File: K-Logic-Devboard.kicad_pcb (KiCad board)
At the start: 2 copper layers, 21 x 51 mm, 33 parts, among them J1 USB_C_Receptacle_USB2.0_14P, J2 Conn_01x20, J3 Conn_01x20, J4 Conn_01x03, SW1 SW_Push, U1 RP2040, U2 MCP1700x-330xxTT, U3 W25Q16JVZPIQ TR, Y1 12 Mhz

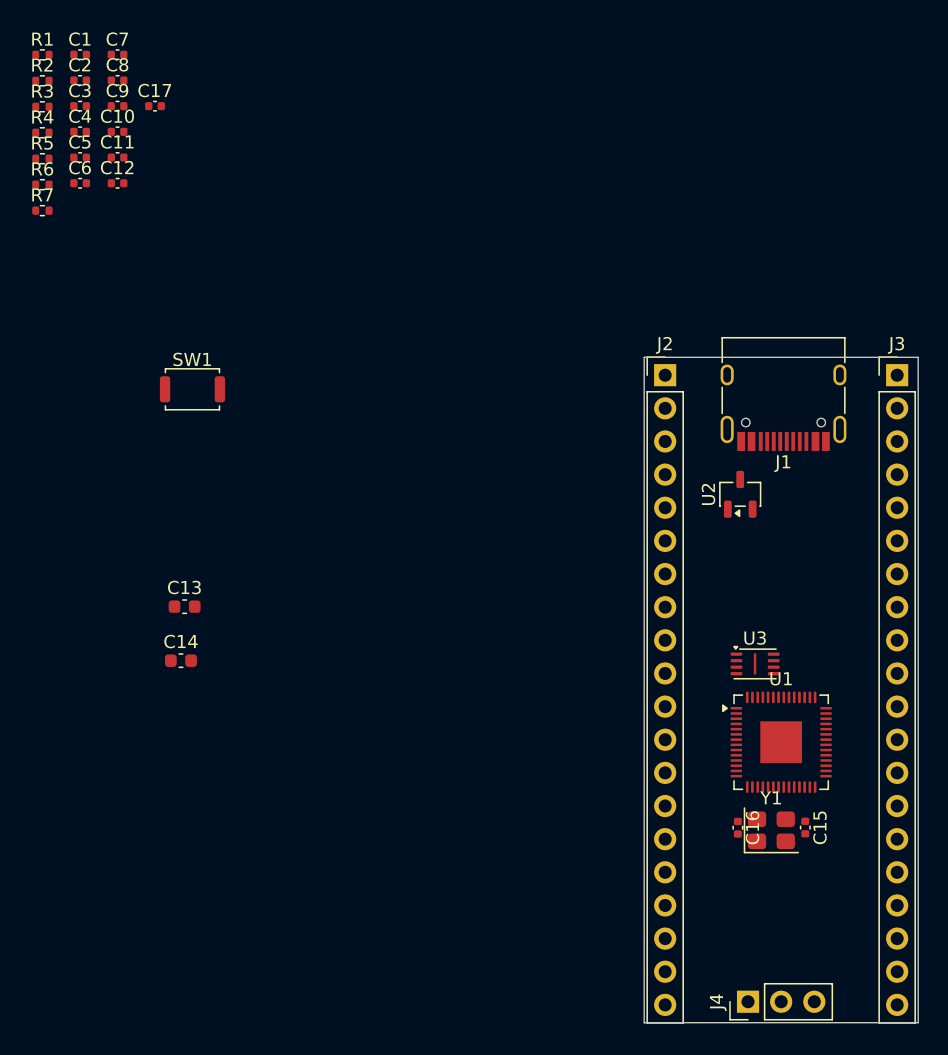
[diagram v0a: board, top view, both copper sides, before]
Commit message: pcb 99.99% done. journals and BOM.
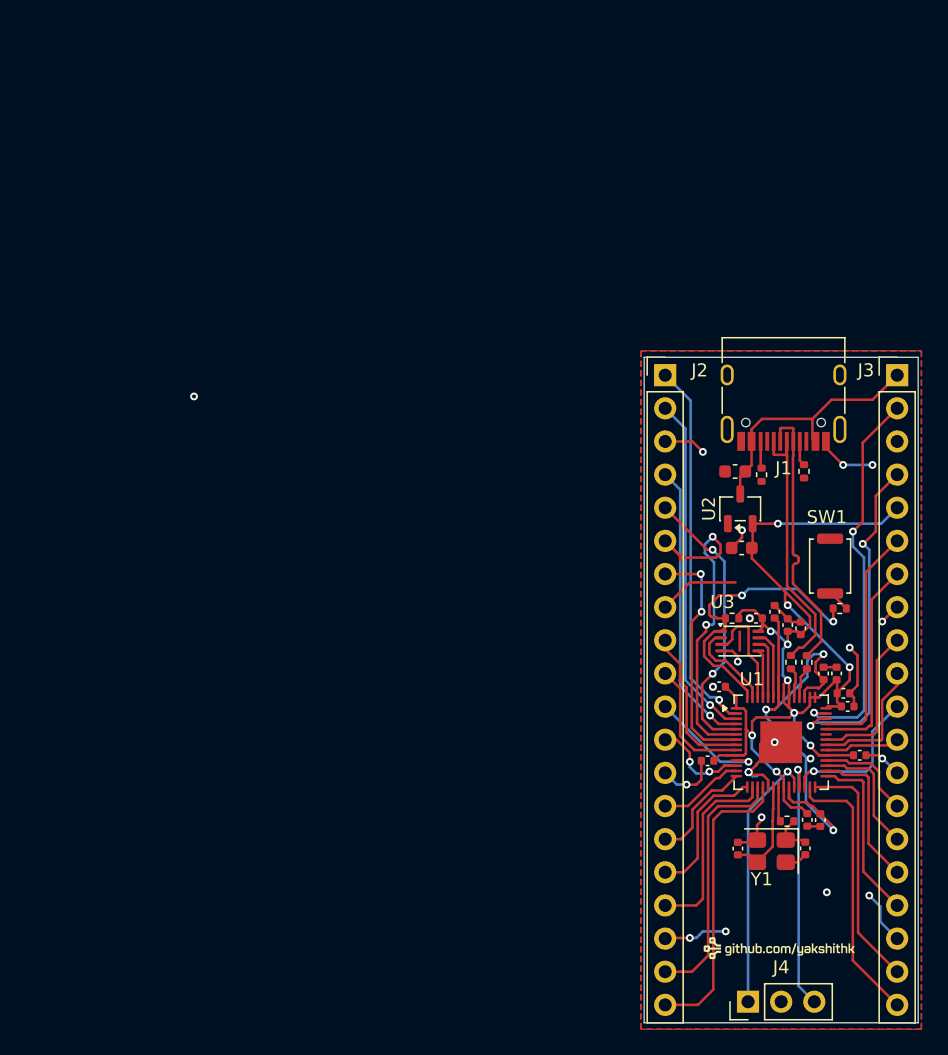
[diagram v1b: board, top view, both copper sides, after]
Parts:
- added G***: LOGO, LOGO, F.Cu at (91.3, 89.3)
- added G***: LOGO, LOGO, B.Cu at (91.8, 68.8)
- moved C8 77.5 mm to (93.5, 79.5), turned to -90 degrees
- moved R5 76.4 mm to (91.9, 79.6), turned to 180 degrees
- moved C1 76.3 mm to (96.3, 69.8)
- moved C2 75.9 mm to (96.6, 70.8)
- moved C5 75.3 mm to (97.5, 74.5)
- moved C11 74.0 mm to (94.5, 79.5), turned to -90 degrees
- moved C7 72.7 mm to (95.8, 68.2), turned to 90 degrees
- moved R3 72.4 mm to (93.5, 67.4), turned to 90 degrees
- moved R4 70.3 mm to (92.2, 67.4), turned to 90 degrees
- moved R6 69.2 mm to (96.0, 63.2), turned to 180 degrees
- moved C3 68.2 mm to (93.0, 64.8), turned to 90 degrees
- moved C10 68.2 mm to (94.8, 68.2), turned to 90 degrees
- moved R1 66.5 mm to (93.2, 52.7), turned to -90 degrees
- moved C4 66.1 mm to (92.0, 64.5), turned to 90 degrees
- moved C6 65.4 mm to (85.9, 74.9), turned to 180 degrees
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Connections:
- R3 pad 2: USB_D+ -> USB_D-
- R4 pad 2: USB_D- -> USB_D+
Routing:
- net +3V3: track 0.00 -> 87.8 mm, vias 0 -> 10
- net GND: track 0.00 -> 58.1 mm, vias 0 -> 19
- net +1V1: track 0.00 -> 38.3 mm, vias 0 -> 4
- net GPIO29_ADC3: track 0.00 -> 30.1 mm, vias 0 -> 2
- net GPIO0: track 0.00 -> 28.8 mm, vias 0 -> 1
- net GPIO4: track 0.00 -> 27.4 mm, vias 0 -> 2
- net GPIO1: track 0.00 -> 26.6 mm, vias 0 -> 1
- net GPIO28_ADC2: track 0.00 -> 25.9 mm, vias 0 -> 2
- net QSPI_SS: track 0.00 -> 23.0 mm, vias 0 -> 2
- net GPIO15: track 0.00 -> 22.7 mm
- net GPIO2: track 0.00 -> 22.2 mm, vias 0 -> 1
- net GPIO3: track 0.00 -> 21.9 mm, vias 0 -> 2
- net USB_D+: track 0.00 -> 21.8 mm
- net USB_D-: track 0.00 -> 21.7 mm
- net GPIO16: track 0.00 -> 20.9 mm
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- added copper zone on F.Cu, net (none)
- added copper zone on B.Cu, net GND
- added copper zone on F.Cu, net GND
